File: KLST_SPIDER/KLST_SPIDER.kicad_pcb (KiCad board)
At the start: 2 copper layers, 100 x 100 mm, 21 parts, among them J1 MIDI_IN, J10 UART, J11 UART, J12 UART, J2 MIDI_OUT, J3 UART, J4 UART, J5 UART, J6 UART, J7 UART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

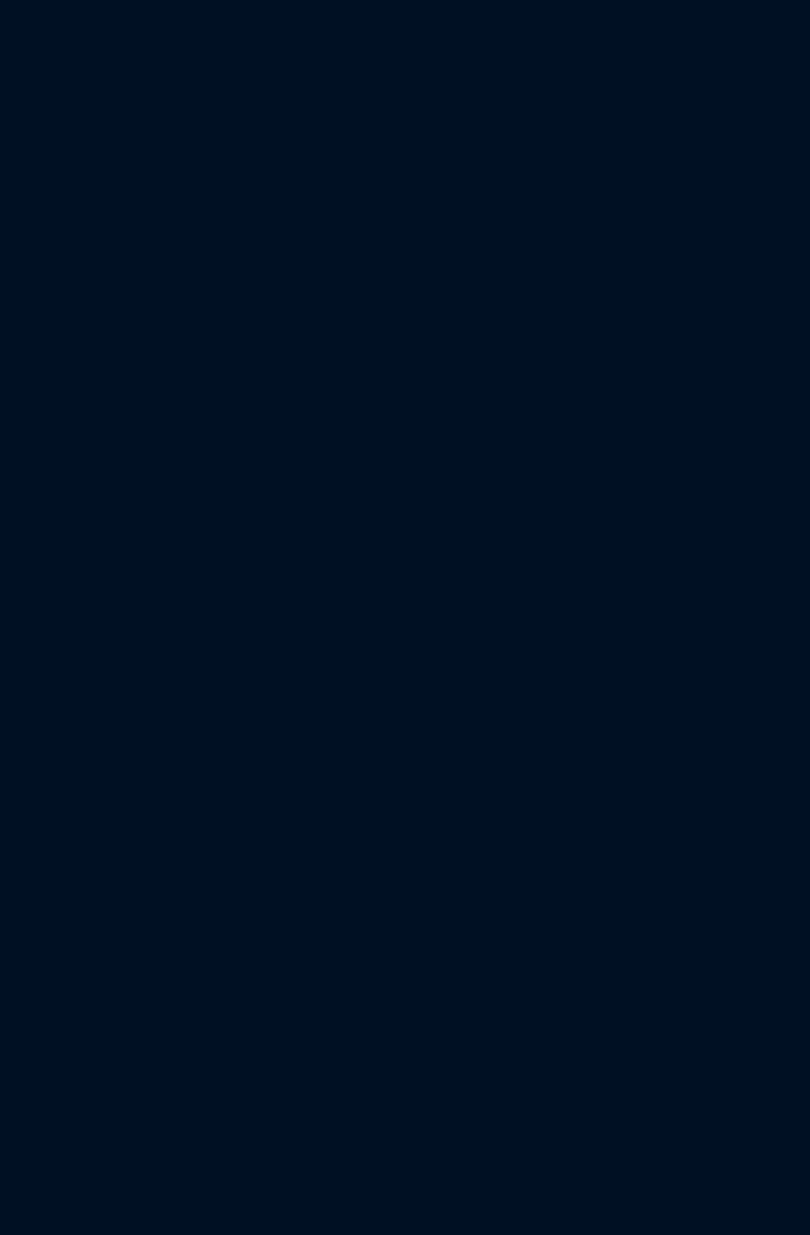
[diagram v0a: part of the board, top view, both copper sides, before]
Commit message: added MIDI THRU
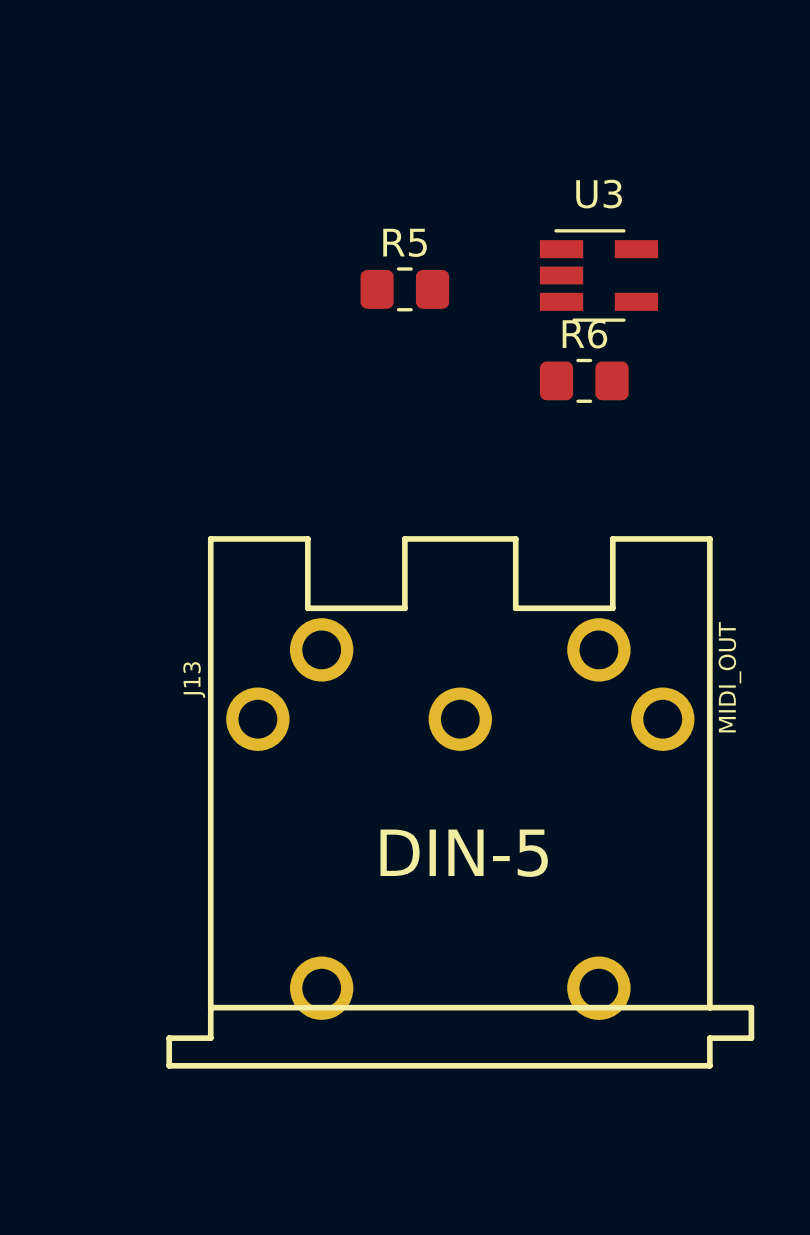
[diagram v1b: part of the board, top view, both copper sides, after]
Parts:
- added J13: MIDI_OUT, DIN-5:DIN5-RA-PTH, F.Cu at (192.0, 137.0)
- added R5: 47, Resistor_SMD:R_0805_2012Metric_Pad1.20x1.40mm_HandSolder, F.Cu at (190.0, 109.0)
- added R6: 47, Resistor_SMD:R_0805_2012Metric_Pad1.20x1.40mm_HandSolder, F.Cu at (196.5, 112.3)
- added U3: 74AHC1G125, Package_TO_SOT_SMD:SOT-23-5_HandSoldering, F.Cu at (197.0, 108.5)
- J1, J2: footprint DIN-5:SparkFun-KiCad-Libraries-master_Footprints_Connectors.pretty_DIN5-RA-PTH -> DIN-5:DIN5-RA-PTH

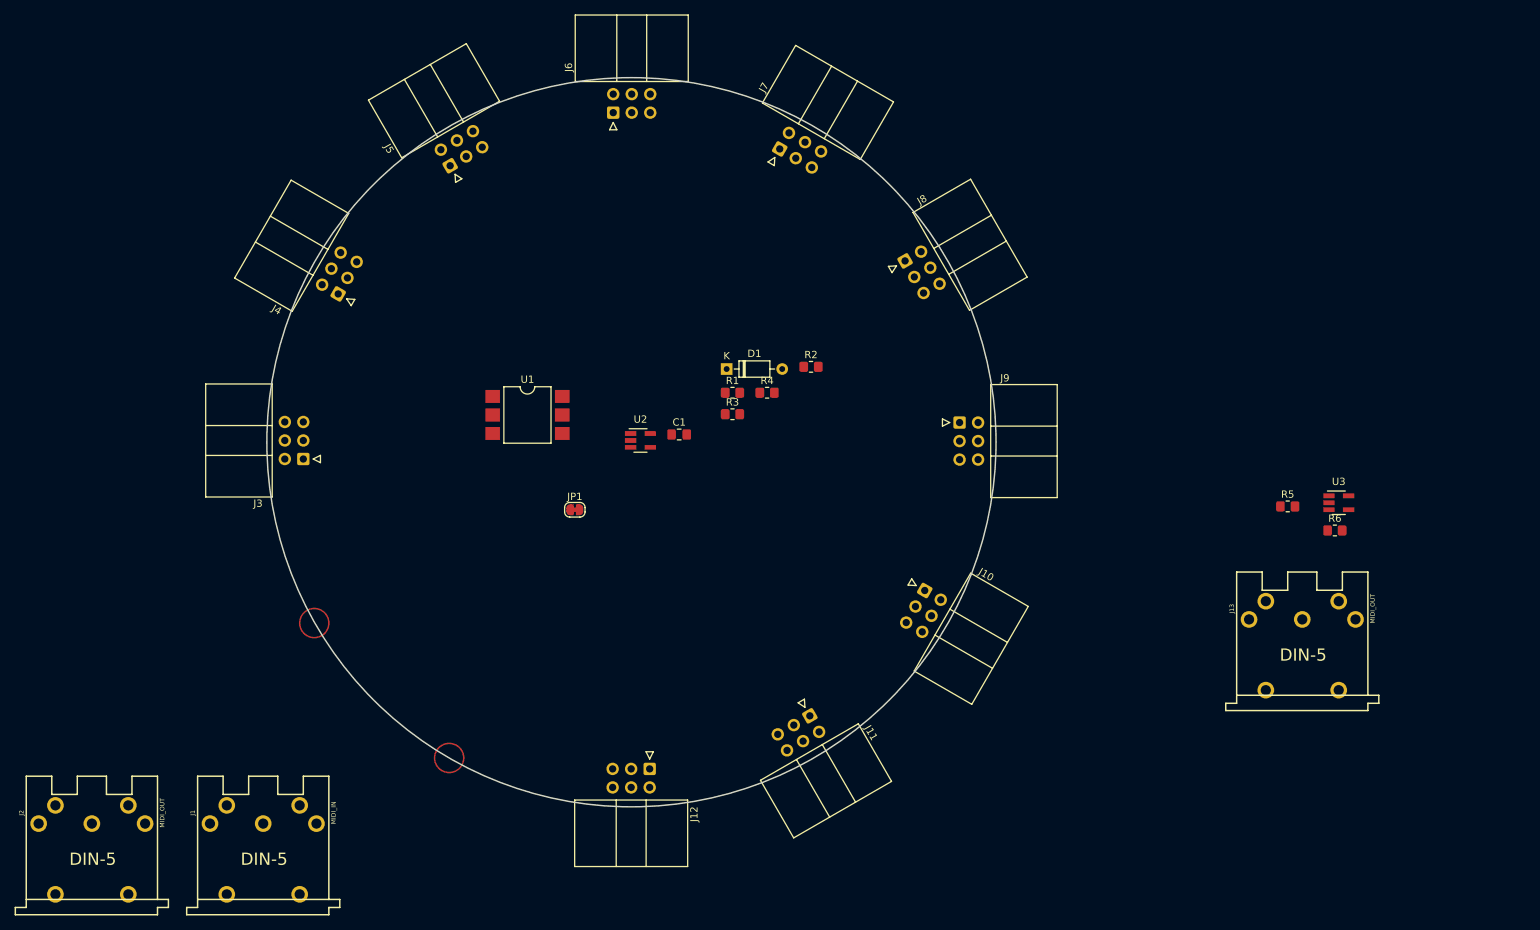
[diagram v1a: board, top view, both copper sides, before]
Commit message: rearranged connectors
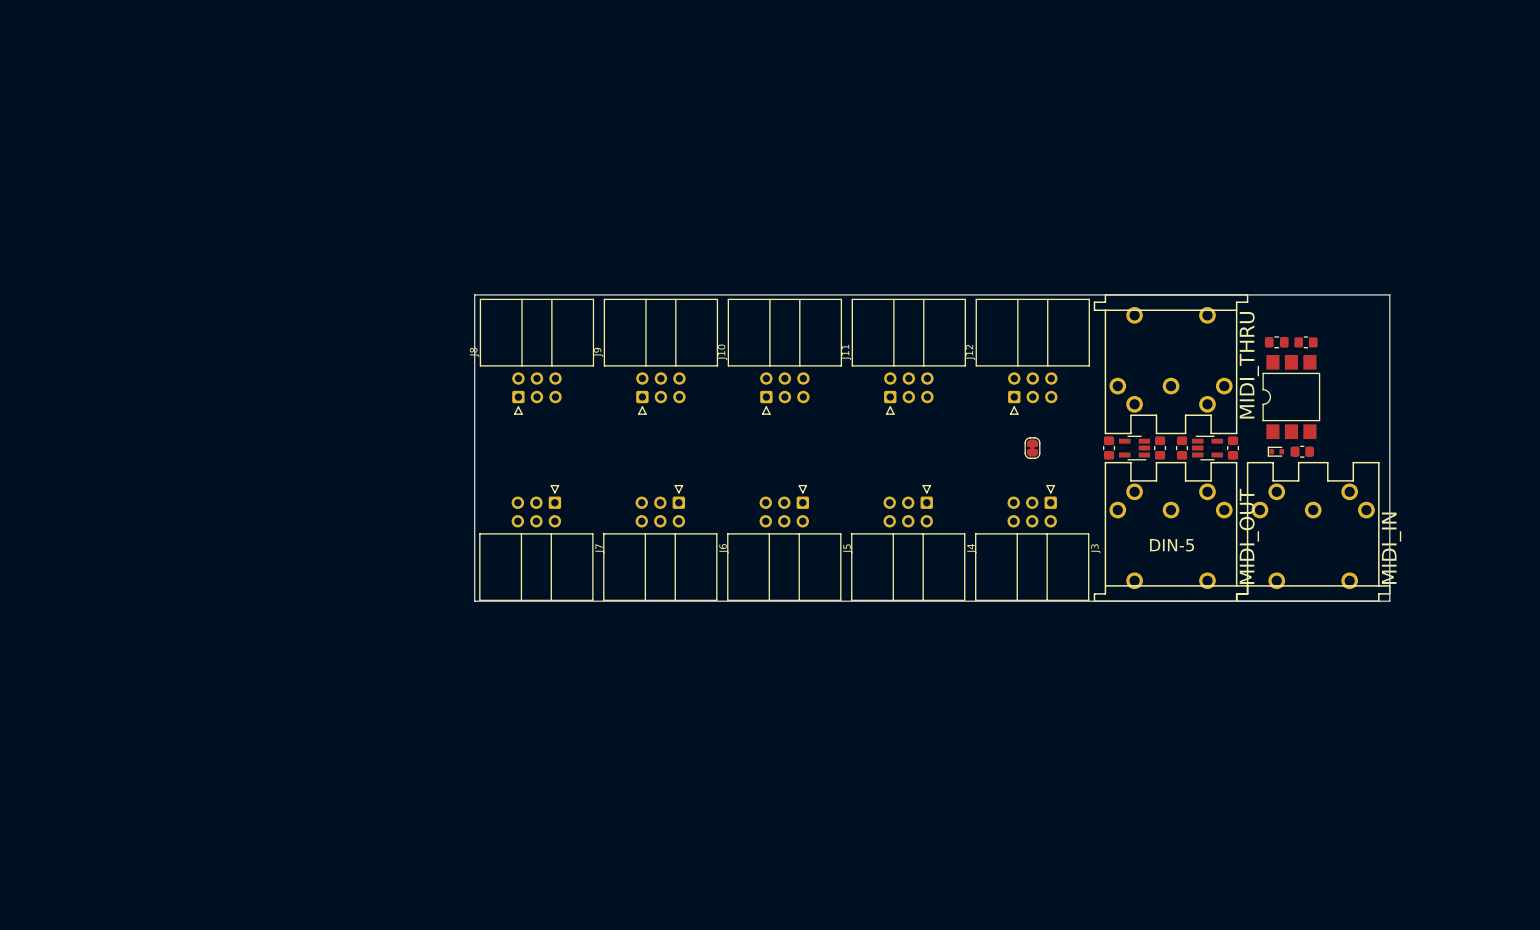
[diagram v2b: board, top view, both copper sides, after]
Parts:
- D1: value 1N914 -> 1N914WT; footprint Diode_THT:D_DO-35_SOD27_P7.62mm_Horizontal -> Diode_SMD:D_SOD-523
- J13: value MIDI_OUT -> MIDI_THRU
- moved J2 154.1 mm to (174.0, 122.0)
- moved J1 150.3 mm to (193.5, 122.0)
- moved U1 104.8 mm to (190.5, 94.0), turned to 90 degrees
- moved J3 102.7 mm to (157.5, 108.5), turned to -90 degrees
- moved J4 85.7 mm to (140.5, 108.5), turned to -90 degrees
- moved C1 82.9 mm to (188.5, 86.5)
- moved D1 76.3 mm to (188.5, 101.5)
- moved R4 74.2 mm to (192.5, 86.5)
- moved J12 71.4 mm to (152.5, 94.0), turned to 90 degrees
- moved R2 68.4 mm to (192.0, 101.5), turned to 180 degrees
- moved U2 67.8 mm to (169.0, 101.0), turned to 180 degrees
- moved J5 66.9 mm to (123.5, 108.5), turned to -90 degrees
- moved JP1 63.3 mm to (155.0, 101.0), turned to 90 degrees
- moved J13 59.8 mm to (174.0, 80.0), turned to 180 degrees
- moved R1 59.1 mm to (172.5, 101.0), turned to -90 degrees
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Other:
- board size 100 x 100 mm -> 125.5 x 42 mm

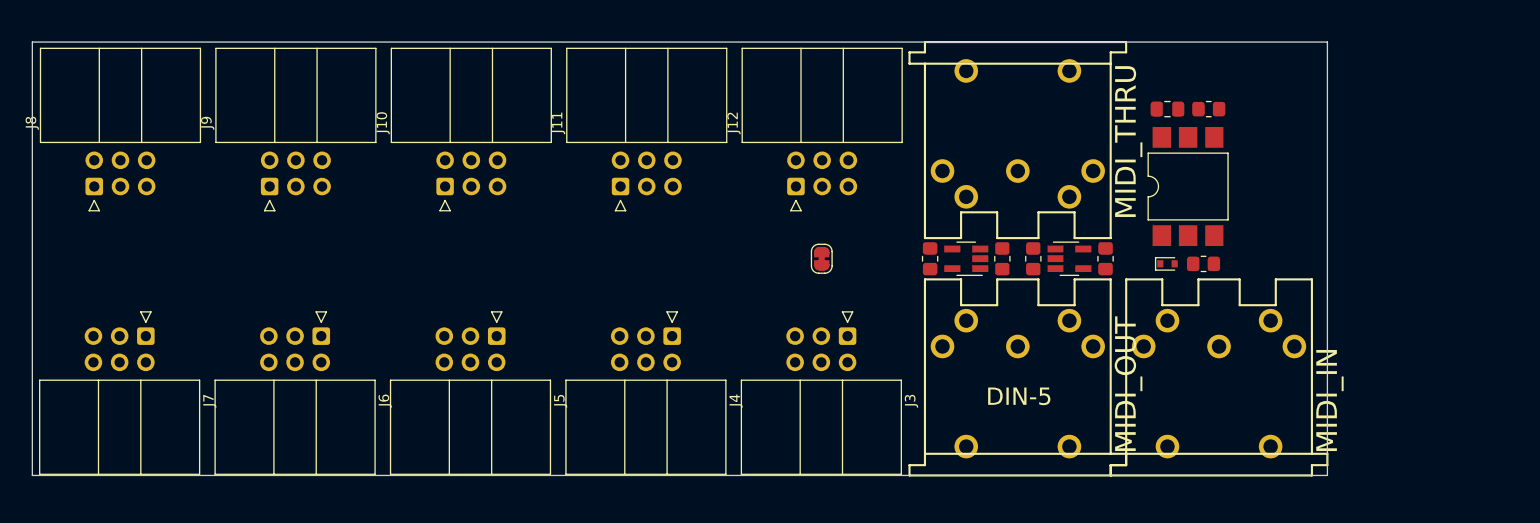
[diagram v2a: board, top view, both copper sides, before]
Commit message: rearranged connectors
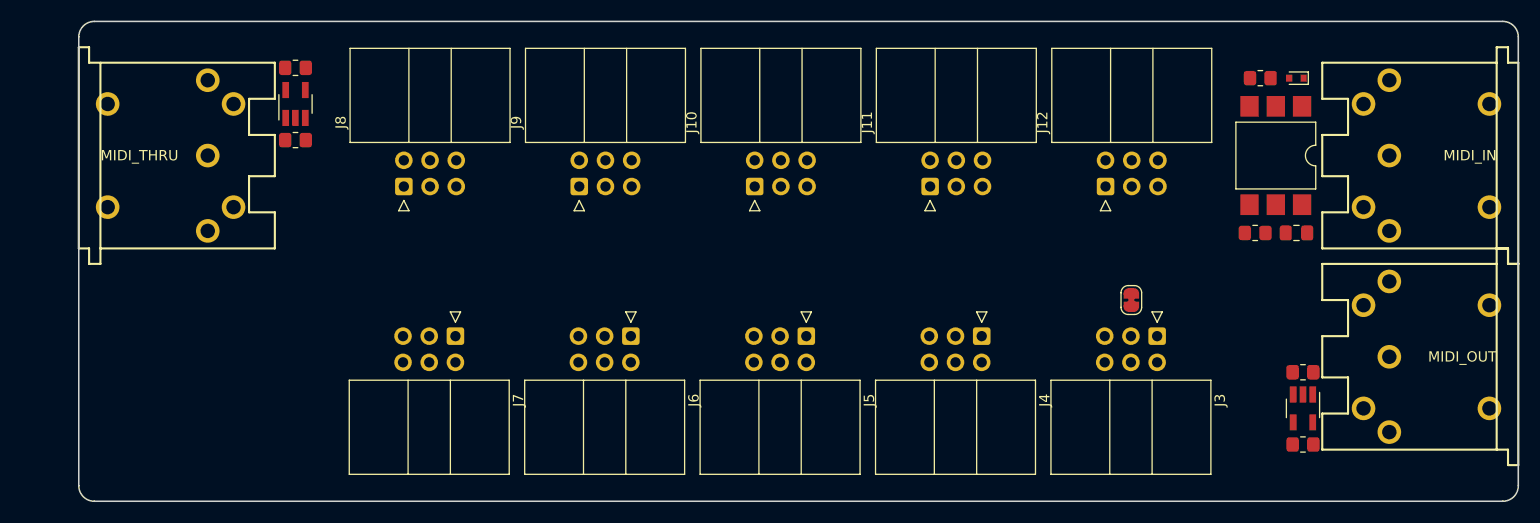
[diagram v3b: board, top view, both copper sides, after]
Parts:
- moved J13 91.7 mm to (83.0, 91.0), turned to -90 degrees
- moved R6 80.7 mm to (104.0, 82.5), turned to 0 degrees
- moved U3 76.5 mm to (104.0, 86.0), turned to 90 degrees
- moved R5 72.4 mm to (104.0, 89.5), turned to 180 degrees
- moved J2 49.8 mm to (222.5, 110.5), turned to 90 degrees
- moved J1 42.4 mm to (222.5, 91.0), turned to 90 degrees
- moved R3 40.4 mm to (201.6, 119.0), turned to 180 degrees
- moved U2 35.7 mm to (201.6, 115.5), turned to -90 degrees
- moved R1 31.1 mm to (201.6, 112.0), turned to 0 degrees
- moved JP1 30.3 mm to (185.0, 105.0)
- moved J10 30.0 mm to (148.5, 94.0)
- moved J11 30.0 mm to (165.5, 94.0)
- moved J12 30.0 mm to (182.5, 94.0)
- moved J3 30.0 mm to (187.5, 108.5)
- moved J4 30.0 mm to (170.5, 108.5)
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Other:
- board size 125.5 x 42 mm -> 139.5 x 46.5 mm

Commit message: prepared JLPCPB production
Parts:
- removed the J4 at (170.5, 108.5)
- added D10: Schottky, Diode_SMD:D_SOD-123, F.Cu at (122.0, 92.0)
- added D2: Schottky, Diode_SMD:D_SOD-123, F.Cu at (158.5, 109.5)
- added D3: Schottky, Diode_SMD:D_SOD-123, F.Cu at (142.0, 109.5)
- added D4: Schottky, Diode_SMD:D_SOD-123, F.Cu at (125.5, 109.5)
- added D5: Schottky, Diode_SMD:D_SOD-123, F.Cu at (109.0, 109.5)
- added D6: Schottky, Diode_SMD:D_SOD-123, F.Cu at (188.0, 92.0)
- added D7: Schottky, Diode_SMD:D_SOD-123, F.Cu at (171.5, 92.0)
- added D8: Schottky, Diode_SMD:D_SOD-123, F.Cu at (155.0, 92.0)
- added D9: Schottky, Diode_SMD:D_SOD-123, F.Cu at (138.5, 92.0)
- added J3: MIDI_THRU, DIN-5:DIN5-RA-PTH, F.Cu at (83.0, 91.0)
- J13: value MIDI_THRU -> UART; footprint DIN-5:DIN5-RA-PTH -> Connector_IDC:IDC-Header_2x03_P2.54mm_Horizontal
- U1: value H11L1 -> H11L1SR2M
- moved J12 53.0 mm to (129.5, 93.5)
- moved J9 47.5 mm to (179.0, 93.5)
- moved J13 30.1 mm to (113.0, 93.5), turned to 90 degrees
- moved J11 19.5 mm to (146.0, 93.5)
- moved J1 19.5 mm to (222.5, 110.5)
- moved J2 19.5 mm to (222.5, 91.0)
- moved J7 15.0 mm to (134.5, 108.0)
- moved J6 14.5 mm to (151.0, 108.0)
- moved J8 14.4 mm to (118.0, 108.0), turned to -90 degrees
- moved J10 14.0 mm to (162.5, 93.5)
- moved J5 14.0 mm to (167.5, 108.0)
- moved JP1 10.1 mm to (176.0, 109.5)
- moved J4 3.54 mm to (184.0, 108.0)
- moved R1 0.63 mm to (201.0, 112.0)
- moved R4 0.63 mm to (201.0, 119.0)
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- renumbered J3 to J4, R5 to R2, R2 to R3, R3 to R4, R6 to R5, R4 to R6
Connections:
- J1 pad 6: (no net) -> unconnected-(J1-Pad6)
- J1 pad 7: (no net) -> unconnected-(J1-Pad7)
- J10 pad 3: /PWR -> Net-(D7-Pad1)
- J10 pad 4: /PWR -> Net-(D7-Pad1)
- J11 pad 3: /PWR -> Net-(D8-Pad1)
- J11 pad 4: /PWR -> Net-(D8-Pad1)
- J12 pad 3: /PWR -> Net-(D9-Pad1)
- J12 pad 4: /PWR -> Net-(D9-Pad1)
- J13 pad 1: unconnected-(J13-Pad1) -> GND
- J13 pad 2: GND -> /UART_RX
- J13 pad 3: unconnected-(J13-Pad3) -> Net-(D10-Pad1)
- J13 pad 4: Net-(J13-Pad4) -> Net-(D10-Pad1)
- J13 pad 5: Net-(J13-Pad5) -> /UART_TX
- J13 pad 6: (no net) -> GND
- J2 pad 6: (no net) -> unconnected-(J2-Pad6)
- J2 pad 7: (no net) -> unconnected-(J2-Pad7)
- J5 pad 3: /PWR -> Net-(D2-Pad1)
- J5 pad 4: /PWR -> Net-(D2-Pad1)
- J6 pad 3: /PWR -> Net-(D3-Pad1)
- J6 pad 4: /PWR -> Net-(D3-Pad1)
- J7 pad 3: /PWR -> Net-(D4-Pad1)
- J7 pad 4: /PWR -> Net-(D4-Pad1)
- J8 pad 3: /PWR -> Net-(D5-Pad1)
- J8 pad 4: /PWR -> Net-(D5-Pad1)
- J9 pad 3: /PWR -> Net-(D6-Pad1)
- J9 pad 4: /PWR -> Net-(D6-Pad1)
- R2 pad 2: Net-(J13-Pad4) -> Net-(J3-Pad4)
- R5 pad 1: Net-(J13-Pad5) -> Net-(J3-Pad5)
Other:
- board size 139.5 x 46.5 mm -> 139.5 x 43.5 mm
- board text added: "MAIN"
